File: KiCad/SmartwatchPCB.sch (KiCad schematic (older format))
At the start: 38 parts, among them IC1 SAML22G, IC2 TFBS4711, J1 USB_B_Micro, J2 Conn_01x04_Male, J3 Conn_01x04_Male, U1 LCD

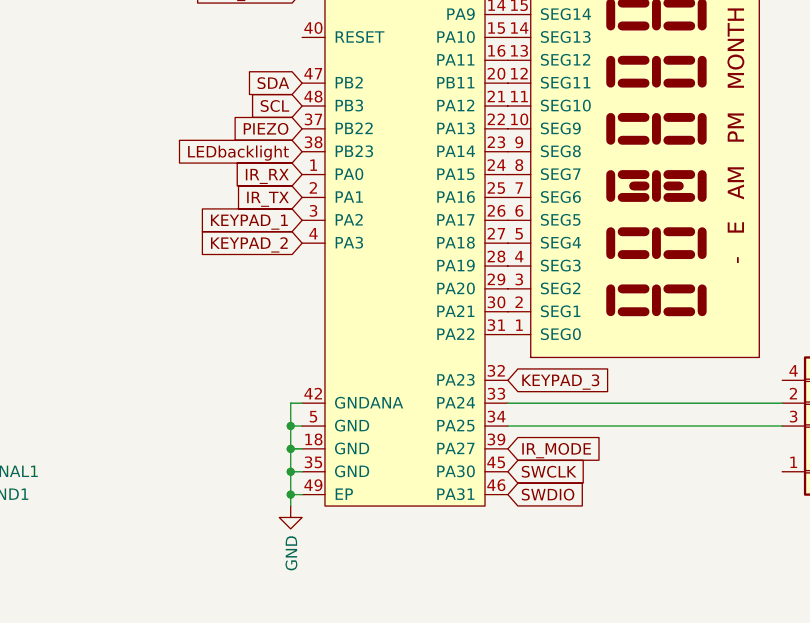
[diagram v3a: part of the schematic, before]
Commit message: moved IC, more wiring
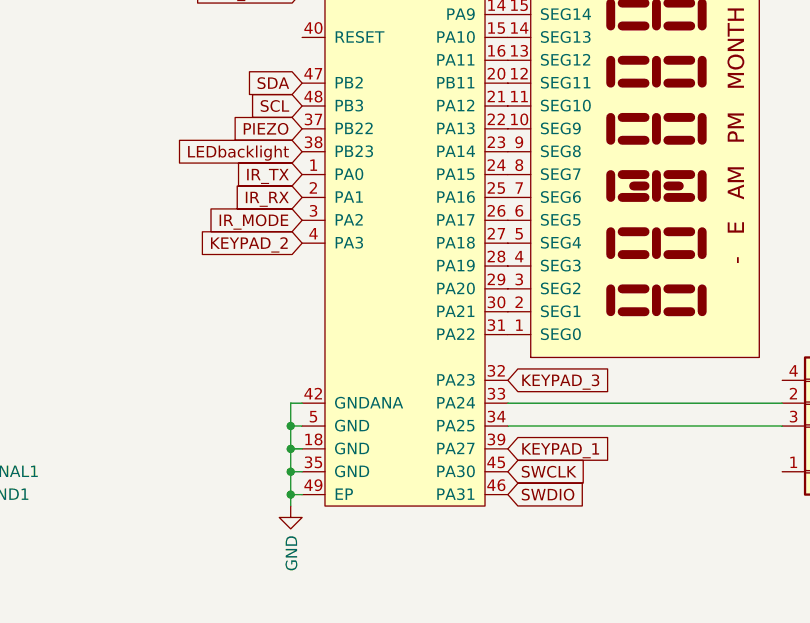
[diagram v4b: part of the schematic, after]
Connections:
- net IR_MODE: now also IC1.3 (PA2); no longer IC1.39 (PA27)
- net IR_RX: now also IC1.2 (PA1); no longer IC1.1 (PA0)
- net IR_TX: now also IC1.1 (PA0); no longer IC1.2 (PA1)
- net KEYPAD_1: now also IC1.39 (PA27); no longer IC1.3 (PA2)
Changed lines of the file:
@@
 	1    0    0    -1
 $EndComp
-Text GLabel 3000 3700 0    50   Input ~ 0
+Text GLabel 3900 4700 2    50   Input ~ 0
 KEYPAD_1
 Text GLabel 3000 3800 0    50   Input ~ 0
@@
 Text GLabel 3000 3300 0    50   Input ~ 0
 PIEZO
+Text GLabel 3000 3600 0    50   Input ~ 0
+IR_RX
 Text GLabel 3000 3500 0    50   Input ~ 0
-IR_RX
-Text GLabel 3000 3600 0    50   Input ~ 0
 IR_TX
 Text GLabel 3000 2700 0    50   Input ~ 0
@@
 Text GLabel 6000 3200 0    50   Input ~ 0
 IR_MODE
-Text GLabel 3900 4700 2    50   Input ~ 0
+Text GLabel 3000 3700 0    50   Input ~ 0
 IR_MODE
 $EndSCHEMATC

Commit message: close to ordering first version
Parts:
- added C5, C6, C7: 100nF, Capacitor_SMD:C_0603_1608Metric, symbol Device:C
- added D2: LED, LED_SMD:LED_0603_1608Metric_Castellated, symbol Device:LED
- added R4, R5: R, Resistor_SMD:R_0603_1608Metric, symbol Device:R
- added TP_GND1, TP_VBAT1: TestPoint, TestPoint:TestPoint_Pad_D1.5mm, symbol Connector:TestPoint
- added U2: MCP73831-2-OT, Package_TO_SOT_SMD:SOT-23-5, symbol Battery_Management:MCP73831-2-OT
- added U3: AP2112K-2.5, Package_TO_SOT_SMD:SOT-23-5, symbol Regulator_Linear:AP2112K-2.5
- U1: footprint SmartwatchPCB:display -> SmartwatchPCB:display_MOUNT
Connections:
- net GND: now also C5.2, C6.2, C7.2, R4.2, TP_GND1.1, U2.2 (VSS), U3.2 (GND)
- net VCC: now also C7.1, U3.5 (VOUT)
- net VBUS: now reaches J1.1 (VBUS)
- net VBUS: now also C5.1, R5.2, U2.4 (VDD)
- new net: D2.1 (K), U2.1 (STAT)
- new net: R4.1, U2.5 (PROG)
- new net: D2.2 (A), R5.1
- new net VBAT: C6.1, TP_VBAT1.1, U2.3 (VBAT), U3.1 (VIN), U3.3 (EN)

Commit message: swapped IR MODE to BAT ANALOG IN
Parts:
- added R6, R7, R8, R9: R, Resistor_SMD:R_0603_1608Metric, symbol Device:R
- added TP_RST1: TestPoint, TestPoint:TestPoint_Pad_D1.5mm, symbol Connector:TestPoint
- J3: footprint Connector_PinHeader_1.27mm:PinHeader_1x04_P1.27mm_Vertical -> Connector_PinHeader_2.54mm:PinHeader_1x04_P2.54mm_Vertical
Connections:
- net GND: now also R9.1
- net SCL: now also R7.1
- net SDA: now also R6.1
- net VBAT: now also R8.2
- net VCC: now also R6.2, R7.2
- net at IC1.40 (RESET): now also TP_RST1.1
- net IR_MODE: no longer names the net of IC1.3 (PA2)
- net IR_MODE: now also R8.1, R9.2; no longer IC2.4 (Shutdown)
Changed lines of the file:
@@
 F 0 "J3" H 9158 3431 50  0000 C CNN
 F 1 "Conn_01x04_Male" H 9158 3340 50  0000 C CNN
-F 2 "Connector_PinHeader_1.27mm:PinHeader_1x04_P1.27mm_Vertical" H 9050 3150 50  0001 C CNN
+F 2 "Connector_PinHeader_2.54mm:PinHeader_1x04_P2.54mm_Vertical" H 9050 3150 50  0001 C CNN
 F 3 "~" H 9050 3150 50  0001 C CNN
 	1    9050 3150
@@
 	2950 4500 2950 4600
 Connection ~ 2950 4600
-Text GLabel 6000 3200 0    50   Input ~ 0
-IR_MODE
-Text GLabel 3000 3700 0    50   Input ~ 0
-IR_MODE
 $Comp
 L Battery_Management:MCP73831-2-OT U2
@@
 	1    0    0    -1
 $EndComp
+$Comp
+L Device:R R7
+U 1 1 6144E078
+P 10550 2850
+F 0 "R7" H 10620 2896 50  0000 L CNN
+F 1 "R" H 10620 2805 50  0000 L CNN
+F 2 "Resistor_SMD:R_0603_1608Metric" V 10480 2850 50  0001 C CNN
+F 3 "~" H 10550 2850 50  0001 C CNN
+	1    10550 2850
+	-1   0    0    1
+$EndComp
+$Comp
+L Device:R R6
+U 1 1 6144EEC6
+P 10150 2850
+F 0 "R6" H 10220 2896 50  0000 L CNN
+F 1 "R" H 10220 2805 50  0000 L CNN
+F 2 "Resistor_SMD:R_0603_1608Metric" V 10080 2850 50  0001 C CNN
+F 3 "~" H 10150 2850 50  0001 C CNN
+	1    10150 2850
+	-1   0    0    1
+$EndComp
+Text GLabel 10550 3000 3    50   Input ~ 0
+SCL
+Text GLabel 10150 3000 3    50   Input ~ 0
+SDA
+$Comp
+L power:VCC #PWR0126
+U 1 1 6144F2E0
+P 10550 2700
+F 0 "#PWR0126" H 10550 2550 50  0001 C CNN
+F 1 "VCC" V 10565 2828 50  0000 L CNN
+F 2 "" H 10550 2700 50  0001 C CNN
+F 3 "" H 10550 2700 50  0001 C CNN
+	1    10550 2700
+	1    0    0    -1
+$EndComp
+$Comp
+L power:VCC #PWR0127
+U 1 1 6144F62C
+P 10150 2700
+F 0 "#PWR0127" H 10150 2550 50  0001 C CNN
+F 1 "VCC" V 10165 2828 50  0000 L CNN
+F 2 "" H 10150 2700 50  0001 C CNN
+F 3 "" H 10150 2700 50  0001 C CNN
+	1    10150 2700
+	1    0    0    -1
+$EndComp
+$Comp
+L Device:R R8
+U 1 1 614924CD
+P 2100 3500
+F 0 "R8" H 2170 3546 50  0000 L CNN
+F 1 "R" H 2170 3455 50  0000 L CNN
+F 2 "Resistor_SMD:R_0603_1608Metric" V 2030 3500 50  0001 C CNN
+F 3 "~" H 2100 3500 50  0001 C CNN
+	1    2100 3500
+	-1   0    0    1
+$EndComp
+$Comp
+L Device:R R9
+U 1 1 614928A9
+P 2100 3900
+F 0 "R9" H 2170 3946 50  0000 L CNN
+F 1 "R" H 2170 3855 50  0000 L CNN
+F 2 "Resistor_SMD:R_0603_1608Metric" V 2030 3900 50  0001 C CNN
+F 3 "~" H 2100 3900 50  0001 C CNN
+	1    2100 3900
+	-1   0    0    1
+$EndComp
+$Comp
+L power:GND #PWR0128
+U 1 1 61492F74
+P 2100 4050
+F 0 "#PWR0128" H 2100 3800 50  0001 C CNN
+F 1 "GND" V 2105 3922 50  0000 R CNN
+F 2 "" H 2100 4050 50  0001 C CNN
+F 3 "" H 2100 4050 50  0001 C CNN
+	1    2100 4050
+	1    0    0    -1
+$EndComp
+Wire Wire Line
+	3000 3700 2100 3700
+Wire Wire Line
+	2100 3700 2100 3650
+Wire Wire Line
+	2100 3750 2100 3700
+Connection ~ 2100 3700
+Text GLabel 2100 3350 1    50   Input ~ 0
+VBAT
+$Comp
+L Connector:TestPoint TP_RST1
+U 1 1 613EC1BA
+P 3000 2900
+F 0 "TP_RST1" H 2650 3100 50  0000 L CNN
+F 1 "TestPoint" V 3045 3088 50  0001 L CNN
+F 2 "TestPoint:TestPoint_Pad_D1.5mm" H 3200 2900 50  0001 C CNN
+F 3 "~" H 3200 2900 50  0001 C CNN
+	1    3000 2900
+	0    -1   -1   0
+$EndComp
 $EndSCHEMATC
